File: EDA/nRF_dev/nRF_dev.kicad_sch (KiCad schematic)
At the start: 44 parts, among them J1 USB_B_Micro, J5 OV7675_DBG, J6 FH26W-25S-0.3SHW(60), U4 OV7675pcb

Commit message: working on nrf camera board
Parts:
- added J4, J7: Conn_01x08_Male, Connector_PinHeader_2.54mm:PinHeader_1x08_P2.54mm_Vertical, symbol Connector:Conn_01x08_Male
- added J8: Conn_01x32_Male, Connector_PinHeader_2.54mm:PinHeader_1x32_P2.54mm_Vertical, symbol Connector:Conn_01x32_Male
- added JP3: ., Jumper:SolderJumper-3_P1.3mm_Open_RoundedPad1.0x1.5mm, symbol Jumper:SolderJumper_3_Open
- added U1: 23LCV1024-I/SN, Package_SO:SOIC-8_3.9x4.9mm_P1.27mm, symbol project:23LCV1024-I/SN
- gave numbers to parts that had none: 29
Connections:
- net +BATT: now also JP3.3 (B)
- net -BATT: now also J4.1 (Pin_1), J4.3 (Pin_3), J4.5 (Pin_5), J4.7 (Pin_7), J7.1 (Pin_1), J7.3 (Pin_3), J7.5 (Pin_5), J7.7 (Pin_7), U1.4 (VSS), U1.7 (VBAT)
- net CB_D0: now also U3.95 (P0.00), J8.1 (Pin_1)
- net CB_D1: now also U3.96 (P0.01), J8.2 (Pin_2)
- net CB_D2: now also U3.97 (P0.02), J8.3 (Pin_3)
- net CB_D3: now also U3.99 (P0.03), J8.4 (Pin_4)
- net CB_D4: now also U3.100 (P0.04), J8.5 (Pin_5)
- net CB_D5: now also U3.2 (P0.05), J8.6 (Pin_6)
- net CB_D6: now also U3.3 (P0.06), J8.7 (Pin_7)
- net CB_D7: now also U3.4 (P0.07), J8.8 (Pin_8)
- net CB_VIN: now also U3.15 (P0.08), J8.9 (Pin_9)
- net FLASH_CS: now also U3.87 (P0.29), J8.30 (Pin_30)
- net FLASH_MISO: now also U3.84 (P0.27), J8.28 (Pin_28)
- net FLASH_MOSI: now also U3.86 (P0.28), J8.29 (Pin_29)
- net FLASH_SCLK: now also U3.83 (P0.26), J8.27 (Pin_27)
- net HREF: now also U3.20 (P0.12), J8.13 (Pin_13)
- net PCLK: now also U3.23 (P0.13_AIN0), J8.14 (Pin_14)
- net PDN: now also U3.26 (P0.16_AIN3), J8.17 (Pin_17)
- net PEN: now also U3.25 (P0.15_AIN2), J8.16 (Pin_16)
- net SCL: now also U3.16 (P0.09), J8.10 (Pin_10)
- net SDA: now also U3.18 (P0.10), J8.11 (Pin_11)
- net SD_CS: now also U3.42 (P0.25_TRACEDATA3), J8.26 (Pin_26), U1.1 (CS)
- net SD_MISO: now also U3.39 (P0.23_TRACEDATA1), J8.24 (Pin_24), U1.2 (SO)
- net SD_MOSI: now also U3.40 (P0.24_TRACEDATA2), J8.25 (Pin_25), U1.5 (SI)
- net SD_SCLK: now also U3.38 (P0.22_TRACEDATA0), J8.23 (Pin_23), U1.6 (SCK)
- net VPP: now also J4.2 (Pin_2), J4.4 (Pin_4), JP3.2 (C); no longer J1.1 (VBUS)
- net VS: now also U3.19 (P0.11), J8.12 (Pin_12)
- net V_3.3: now also J4.6 (Pin_6), J4.8 (Pin_8), J7.2 (Pin_2), J7.4 (Pin_4), J7.6 (Pin_6), J7.8 (Pin_8), U1.8 (VCC)
- net XCLK: now also U3.24 (P0.14_AIN1), J8.15 (Pin_15)
- net nRF_PWR: now also U3.88 (P0.30), J8.31 (Pin_31)
- net nRF_STAT: now also U3.89 (P0.31), J8.32 (Pin_32)
- net at U3.28 (P0.17_AIN4): now also J8.18 (Pin_18)
- net at U3.29 (P0.18_AIN5): now also J8.19 (Pin_19)
- net at U3.30 (P0.19_AIN6): now also J8.20 (Pin_20)
- net at U3.35 (P0.20_AIN7): now also J8.21 (Pin_21)
- net at U3.37 (P0.21_TRACECLK): now also J8.22 (Pin_22)
- new net V_USB: J1.1 (VBUS), JP3.1 (A)
- no-connect marks 50 -> 24
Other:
- moved on the sheet: C17, C3, J1, J2

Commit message: adding layout work for nrf_dev pcb
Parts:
- added J11: UART, Connector_PinHeader_2.54mm:PinHeader_1x04_P2.54mm_Vertical, symbol Connector_Generic:Conn_01x04
- added SW1: RST, Button_Switch_SMD:SW_Push_1P1T_NO_6x6mm_H9.5mm, symbol Switch:SW_SPST
- C1: value 100 μF -> 100 uF
- C17, C4: value 10u -> 10 uF
- C18, C19: value 100n -> 100 nF
- J1: footprint RP2040_minimal:USB_Micro-B_Amphenol_10103594-0001LF_Horizontal_modified -> Connector_USB:USB_Micro-B_Molex-105017-0001
- J10: footprint SIMFootprints:Pinpads_1.27mm02x03 -> Connector_PinHeader_1.27mm:PinHeader_2x03_P1.27mm_Vertical
- J2: footprint Connector_JST:JST_PH_S2B-PH-SM4-TB_1x02-1MP_P2.00mm_Horizontal -> Connector_BarrelJack:BarrelJack_Horizontal
- J3: footprint SIMFootprints:microSD_Connector -> project:microSD_Connector
- J9: footprint SIMFootprints:SIMNano -> project:SIMNano
- U5: footprint SIMFootprints:TSNP-6-2 -> project:TSNP-6-2
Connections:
- net +3V3 is gone; now on net V_3.3: C17.1, JP1.1 (A)
- net -BATT: now also J11.4 (Pin_4), SW1.1 (A)
- net FLASH_CS: now also U1.1 (CS)
- net FLASH_MISO: now also U1.2 (SO)
- net FLASH_MOSI: now also U1.5 (SI)
- net FLASH_SCLK: now also U1.6 (SCK)
- net SD_CS: no longer U1.1 (CS)
- net SD_MISO: no longer U1.2 (SO)
- net SD_MOSI: no longer U1.5 (SI)
- net SD_SCLK: no longer U1.6 (SCK)
- net nRF_RST: now also J11.3 (Pin_3), SW1.2 (B)
- net TX: now reaches J8.21 (Pin_21), U3.35 (P0.20_AIN7)
- net TX: now also J11.1 (Pin_1)
- net RX: now reaches J8.22 (Pin_22), U3.37 (P0.21_TRACECLK)
- net RX: now also J11.2 (Pin_2)
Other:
- note removed: "RTC"
- moved on the sheet: C5, C6, C8, C9

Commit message: more layout work
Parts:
- removed J8: Conn_01x32_Male, Connector_PinHeader_2.54mm:PinHeader_1x32_P2.54mm_Vertical, symbol Connector:Conn_01x32_Male
- added J8: Conn_01x15_Male, Connector_PinHeader_2.54mm:PinHeader_1x15_P2.54mm_Vertical, symbol Connector:Conn_01x15_Male
- added SW2: BTA, Button_Switch_SMD:SW_Push_1P1T_NO_6x6mm_H9.5mm, symbol Switch:SW_SPST
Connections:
- net nRF_PWR is gone; now on net RX: U3.88 (P0.30)
- net nRF_STAT is gone; now on net TX: U3.89 (P0.31)
- net -BATT: now also SW2.1 (A); no longer C17.2
- net CB_GND: now also C17.2
- net CB_VCC: now also C17.1, R2.1, R5.1
- net FLASH_CS: now also U3.86 (P0.28), J8.12 (Pin_12); no longer U3.87 (P0.29)
- net FLASH_MISO: now also U3.87 (P0.29), J8.13 (Pin_13); no longer U3.84 (P0.27)
- net FLASH_MOSI: now also U3.84 (P0.27), J8.11 (Pin_11); no longer U3.86 (P0.28)
- net FLASH_SCLK: now also J8.10 (Pin_10)
- net RX: now also J8.14 (Pin_14); no longer U3.37 (P0.21_TRACECLK)
- net SD_CS: now also J8.9 (Pin_9)
- net SD_MISO: now also J8.7 (Pin_7)
- net SD_MOSI: now also J8.8 (Pin_8)
- net SD_SCLK: now also J8.6 (Pin_6)
- net TX: now also J8.15 (Pin_15); no longer U3.35 (P0.20_AIN7)
- net V_3.3: no longer C17.1, R2.1, R5.1
- net at U3.28 (P0.17_AIN4): now also J8.1 (Pin_1)
- net at U3.29 (P0.18_AIN5): now also J8.2 (Pin_2)
- net at U3.30 (P0.19_AIN6): now also J8.3 (Pin_3)
- new net: J8.4 (Pin_4), U3.35 (P0.20_AIN7)
- new net BTA: J8.5 (Pin_5), SW2.2 (B), U3.37 (P0.21_TRACECLK)

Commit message: finished layout and gerber files for nRF dev camera
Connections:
- net -BATT: no longer J6.S1 (SHIELD), J6.S2 (SHIELD)
- net CB_GND: now also J6.S1 (SHIELD), J6.S2 (SHIELD)
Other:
- company: Raspberry Pi (Trading) Ltd -> BoSL
- title: RP2040 Minimal Design Example -> BoSL Camera dev
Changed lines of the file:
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@@
   (paper "A3")
   (title_block
-    (title "RP2040 Minimal Design Example")
-    (date "2020-12-18")
-    (rev "REV1")
-    (company "Raspberry Pi (Trading) Ltd")
+    (title "BoSL Camera dev")
+    (date "2022-11-06")
+    (rev "0.0.1")
+    (company "BoSL")
   )
   (junction (at 248.285 165.735) (diameter 0) (color 0 0 0 0)
@@
     (stroke (width 0) (type default) (color 0 0 0 0))
   )
-  (wire (pts (xy 255.27 258.445) (xy 255.27 260.985))
+  (wire (pts (xy 255.27 258.445) (xy 255.27 266.065))
     (stroke (width 0) (type default) (color 0 0 0 0))
   )
@@
     )
   )
+  (global_label "CB_GND" (shape input) (at 255.27 266.065 0) (fields_autoplaced)
+    (effects (font (size 1.27 1.27)) (justify left))
+    (property "Intersheet References" "${INTERSHEET_REFS}" (id 0) (at 264.9723 266.1444 0)
+      (effects (font (size 1.27 1.27)) (justify left) hide)
+    )
+  )
   (global_label "CB_D7" (shape input) (at 158.115 87.63 180) (fields_autoplaced)
     (effects (font (size 1.27 1.27)) (justify right))
@@
     (pin "2")
   )
-  (symbol (lib_id "power:GND") (at 255.27 260.985 0) (unit 1)
-    (in_bom yes) (on_board yes) (fields_autoplaced)
-    (property "Reference" "#PWR026" (id 0) (at 255.27 267.335 0)
-      (effects (font (size 1.27 1.27)) hide)
-    )
-    (property "Value" "GND" (id 1) (at 255.27 265.5475 0))
-    (property "Footprint" "" (id 2) (at 255.27 260.985 0)
-      (effects (font (size 1.27 1.27)) hide)
-    )
-    (property "Datasheet" "" (id 3) (at 255.27 260.985 0)
-      (effects (font (size 1.27 1.27)) hide)
-    )
-    (pin "1")
-  )
   (symbol (lib_id "BoSLnano-rescue:GND-power") (at 398.78 108.585 0) (unit 1)
     (in_bom yes) (on_board yes)
@@
       (reference "#PWR010") (unit 1) (value "GND") (footprint "")
     )
-    (path "/41dbed34-9b8b-45d8-83ff-788619bc7781"
-      (reference "#PWR026") (unit 1) (value "GND") (footprint "")
-    )
     (path "/37f37914-e8e7-48b3-9784-24b435a1454c"

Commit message: fixed pcb errors
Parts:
- removed R6: 1 kΩ, Resistor_SMD:R_0402_1005Metric, symbol BoSLnano-rescue:R-Device
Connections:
- net VPP: now also R4.1
- net V_3.3: no longer R4.1
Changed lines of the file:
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@@
   (title_block
     (title "BoSL Camera dev")
-    (date "2022-11-06")
-    (rev "0.0.1")
+    (date "2022-11-23")
+    (rev "0.0.2")
     (company "BoSL")
   )
@@
   (junction (at 172.72 133.35) (diameter 0) (color 0 0 0 0)
   )
-  (junction (at 229.87 93.345) (diameter 0) (color 0 0 0 0)
-  )
   (junction (at 353.06 95.885) (diameter 0) (color 0 0 0 0)
   )
@@
     (stroke (width 0) (type default) (color 0 0 0 0))
   )
-  (wire (pts (xy 229.87 93.345) (xy 239.395 93.345))
-    (stroke (width 0) (type default) (color 0 0 0 0))
-  )
   (wire (pts (xy 172.72 135.89) (xy 175.26 135.89))
     (stroke (width 0) (type default) (color 0 0 0 0))
@@
     (stroke (width 0) (type default) (color 0 0 0 0))
   )
-  (wire (pts (xy 326.39 169.545) (xy 326.39 163.83))
-    (stroke (width 0) (type default) (color 0 0 0 0))
-  )
   (wire (pts (xy 394.97 98.425) (xy 398.78 98.425))
     (stroke (width 0) (type default) (color 0 0 0 0))
@@
     (stroke (width 0) (type default) (color 0 0 0 0))
   )
-  (wire (pts (xy 239.395 93.345) (xy 239.395 97.155))
+  (wire (pts (xy 239.395 95.25) (xy 239.395 97.155))
     (stroke (width 0) (type default) (color 0 0 0 0))
   )
@@
     )
   )
-  (global_label "V_3.3" (shape input) (at 326.39 156.21 90) (fields_autoplaced)
-    (effects (font (size 1.524 1.524)) (justify left))
-    (property "Intersheet References" "${INTERSHEET_REFS}" (id 0) (at 275.59 -10.16 0)
-      (effects (font (size 1.27 1.27)) hide)
-    )
-  )
   (global_label "SCL" (shape input) (at 266.7 238.125 0) (fields_autoplaced)
     (effects (font (size 1.27 1.27)) (justify left))
@@
     (pin "1")
   )
-  (symbol (lib_id "BoSLnano-rescue:R-Device") (at 326.39 160.02 0) (unit 1)
-    (in_bom yes) (on_board yes)
-    (property "Reference" "R6" (id 0) (at 323.215 159.385 0))
-    (property "Value" "1 kΩ" (id 1) (at 321.945 161.925 0))
-    (property "Footprint" "Resistor_SMD:R_0402_1005Metric" (id 2) (at 324.612 160.02 90)
-      (effects (font (size 1.27 1.27)) hide)
-    )
-    (property "Datasheet" "" (id 3) (at 326.39 160.02 0))
-    (pin "1")
-    (pin "2")
-  )
   (symbol (lib_id "SIM7000-rescue:AT-ant") (at 290.195 87.63 270) (mirror x) (unit 1)
     (in_bom yes) (on_board yes)
@@
     (pin "2")
   )
+  (symbol (lib_id "BoSLnano-rescue:VPP-power") (at 239.395 95.25 0) (unit 1)
+    (in_bom yes) (on_board yes)
+    (property "Reference" "#PWR0103" (id 0) (at 239.395 99.06 0)
+      (effects (font (size 1.27 1.27)) hide)
+    )
+    (property "Value" "VPP" (id 1) (at 239.395 91.44 0))
+    (property "Footprint" "" (id 2) (at 239.395 95.25 0))
+    (property "Datasheet" "" (id 3) (at 239.395 95.25 0))
+    (pin "1")
+  )
   (symbol (lib_id "BoSLnano-rescue:Micro_SD_Card-Connector") (at 48.895 137.16 180) (unit 1)
     (in_bom yes) (on_board yes)
@@
     (pin "97")
     (pin "99")
+    (pin "1")
+    (pin "10")
+    (pin "104")
+    (pin "105")
+    (pin "106")
+    (pin "107")
+    (pin "108")
+    (pin "109")
+    (pin "11")
+    (pin "110")
+    (pin "111")
+    (pin "112")
+    (pin "113")
+    (pin "114")
+    (pin "115")
+    (pin "116")
+    (pin "117")
+    (pin "118")
+    (pin "119")
+    (pin "120")
+    (pin "121")
+    (pin "122")
+    (pin "123")
+    (pin "124")
+    (pin "125")
+    (pin "126")
+    (pin "127")
+    (pin "14")
+    (pin "17")
+    (pin "21")
+    (pin "27")
+    (pin "31")
+    (pin "36")
+    (pin "41")
+    (pin "44")
+    (pin "47")
+    (pin "5")
+    (pin "50")
+    (pin "51")
+    (pin "52")
+    (pin "56")
+    (pin "6")
+    (pin "60")
+    (pin "62")
+    (pin "63")
+    (pin "65")
+    (pin "66")
+    (pin "68")
+    (pin "69")
+    (pin "7")
+    (pin "70")
+    (pin "71")
+    (pin "72")
+    (pin "73")
+    (pin "74")
+    (pin "75")
+    (pin "76")
+    (pin "77")
+    (pin "78")
+    (pin "79")
+    (pin "8")
+    (pin "80")
+    (pin "81")
+    (pin "82")
+    (pin "85")
+    (pin "9")
+    (pin "90")
+    (pin "94")
+    (pin "98")
   )
   (symbol (lib_id "BoSLnano-rescue:CP-Device") (at 58.42 49.53 0) (unit 1)
@@
       (effects (font (size 1.524 1.524)) hide)
     )
+    (pin "100")
+    (pin "101")
+    (pin "102")
+    (pin "103")
+    (pin "12")
+    (pin "13")
+    (pin "15")
+    (pin "16")
+    (pin "18")
+    (pin "19")
+    (pin "2")
+    (pin "20")
+    (pin "22")
+    (pin "23")
+    (pin "24")
+    (pin "25")
+    (pin "26")
+    (pin "28")
+    (pin "29")
+    (pin "3")
+    (pin "30")
+    (pin "32")
+    (pin "33")
+    (pin "34")
+    (pin "35")
+    (pin "37")
+    (pin "38")
+    (pin "39")
+    (pin "4")
+    (pin "40")
+    (pin "42")
+    (pin "43")
+    (pin "45")
+    (pin "46")
+    (pin "48")
+    (pin "49")
+    (pin "53")
+    (pin "54")
+    (pin "55")
+    (pin "57")
+    (pin "58")
+    (pin "59")
+    (pin "61")
+    (pin "64")
+    (pin "67")
+    (pin "83")
+    (pin "84")
+    (pin "86")
+    (pin "87")
+    (pin "88")
+    (pin "89")
+    (pin "91")
+    (pin "92")
+    (pin "93")
+    (pin "95")
+    (pin "96")
+    (pin "97")
+    (pin "99")
     (pin "1")
     (pin "10")
@@
       (reference "#PWR0102") (unit 1) (value "GND") (footprint "")
     )
+    (path "/13496581-9c4a-4023-97de-a6a6bad5a40f"
+      (reference "#PWR0103") (unit 1) (value "VPP") (footprint "")
+    )
     (path "/cbf8ffc8-8d47-4a8d-b9de-646161a7b2a8"
       (reference "#PWR0104") (unit 1) (value "GND") (footprint "")
@@
       (reference "R5") (unit 1) (value "10 kΩ") (footprint "Resistor_SMD:R_0402_1005Metric")
     )
-    (path "/127d9ee2-01d1-498f-ae61-5e2a7396948b"
-      (reference "R6") (unit 1) (value "1 kΩ") (footprint "Resistor_SMD:R_0402_1005Metric")
-    )
     (path "/f5d5bd4a-108f-418f-8859-779e2f50ba63"

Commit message: revision 0.0.3 of the nRF dev board
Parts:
- added D1: LED, LED_SMD:LED_0603_1608Metric_Pad1.05x0.95mm_HandSolder, symbol Device:LED
- added R6, R8: 10 kΩ, Resistor_SMD:R_0402_1005Metric, symbol BoSLnano-rescue:R-Device
- added U7: SIP32508DT-T1-GE3, Package_TO_SOT_SMD:SOT-23-6, symbol project:SIP32508DT-T1-GE3
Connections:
- net -BATT: now also D1.1 (K), U7.4 (GND)
- net CB_D0: now also J5.16 (Pin_16), J6.22, U4.16 (D1); no longer J5.15 (Pin_15), J6.4, U4.15 (D0)
- net CB_D1: now also J5.15 (Pin_15), J6.21, U4.15 (D0); no longer J5.16 (Pin_16), J6.5, U4.16 (D1)
- net CB_D2: now also J6.20; no longer J6.6
- net CB_D3: now also J6.19; no longer J6.7
- net CB_D4: now also J6.18; no longer J6.8
- net CB_D5: now also J6.17; no longer J6.9
- net CB_D6: now also J6.16; no longer J6.10
- net CB_D7: now also J6.15; no longer J6.11
- net CB_GND: now also J6.12, J6.8; no longer J6.14, J6.18
- net CB_VCC: now also J6.6, J6.7; no longer J6.19, J6.20
- net HREF: now also J6.10; no longer J6.16
- net PCLK: now also J6.9; no longer J6.17
- net PDN: now also J6.1; no longer J6.25
- net SCL: now also J6.14; no longer J6.12
- net VS: now also J6.5; no longer J6.21
- net V_3.3: now also U7.5 (IN), U7.6 (IN)
- net XCLK: now also J6.11; no longer J6.15
- net LED: now reaches J8.4 (Pin_4), U3.35 (P0.20_AIN7)
- net LED: now also R6.1, R8.1
- net CB_VIN: no longer names the net of JP1.3 (B)
- net CB_VIN: now also U7.1 (OUT), U7.2 (OUT); no longer U3.15 (P0.08)
- new net: D1.2 (A), R6.2, R8.2
- new net CB_VEN: U3.15 (P0.08), U7.3 (EN)
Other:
- moved on the sheet: C17, C18, C19, J6, JP1, JP2, R2, R5, SW1, SW2

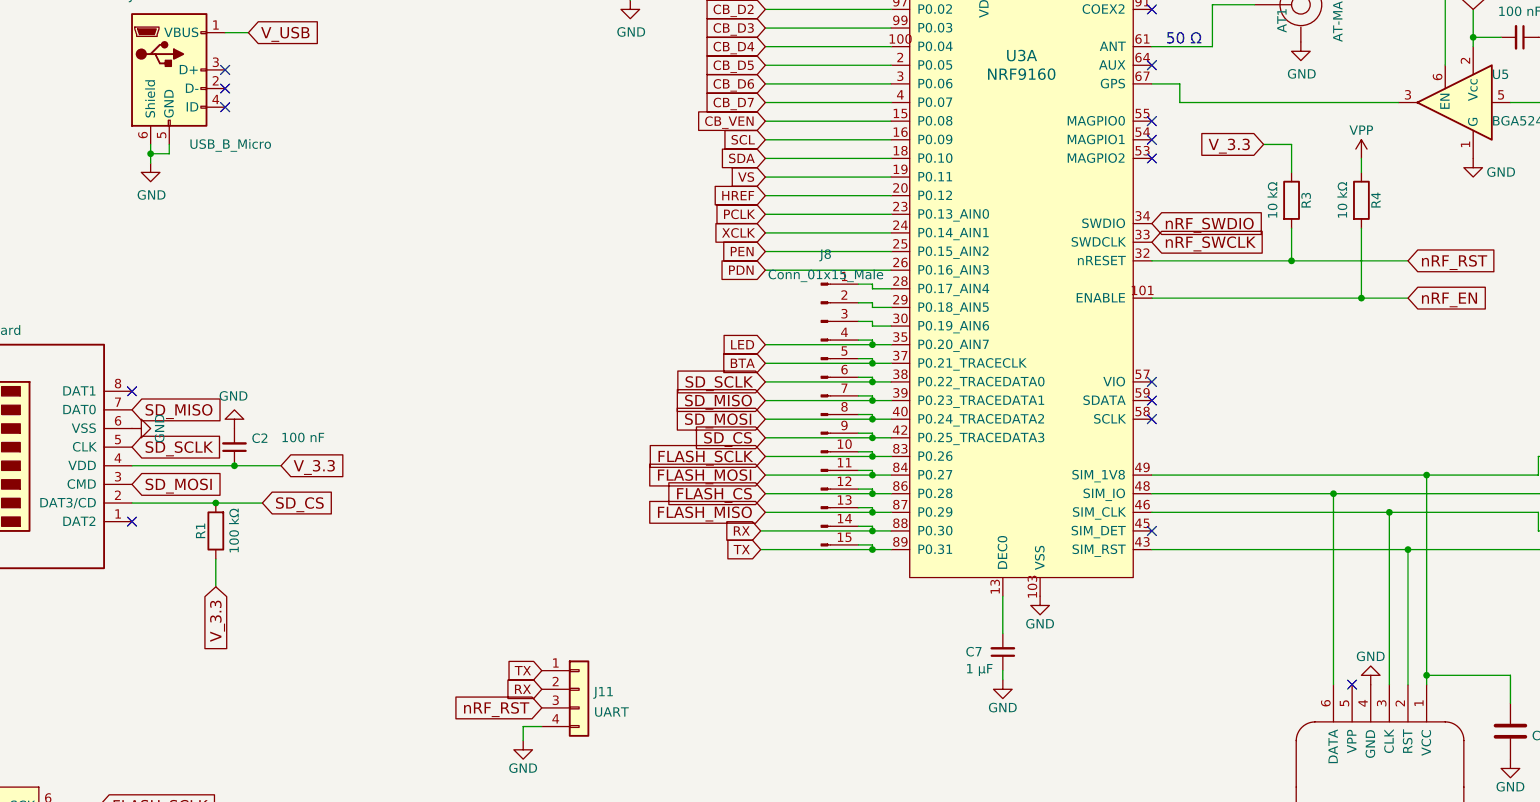
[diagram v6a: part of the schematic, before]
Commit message: updated power saving features
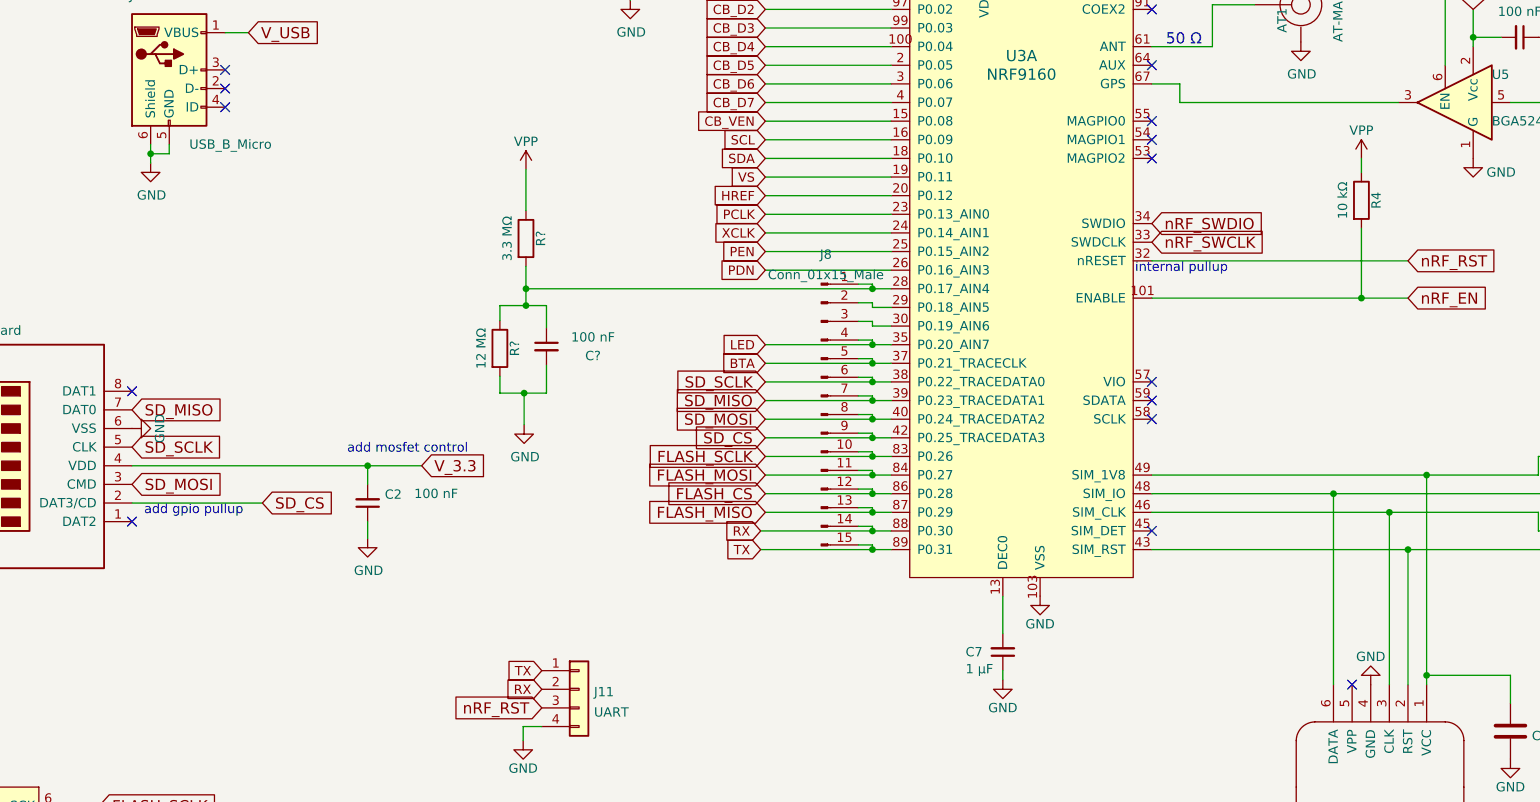
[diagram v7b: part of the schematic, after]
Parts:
- removed R1: 100 kΩ, Resistor_SMD:R_0402_1005Metric, symbol BoSLnano-rescue:R-Device
- removed R3: 10 kΩ, Resistor_SMD:R_0402_1005Metric, symbol BoSLnano-rescue:R-Device
- added C?: 100 nF, Capacitor_SMD:C_0402_1005Metric, symbol BoSLnano-rescue:C_Small-Device
- added R?: 3.3 MΩ, Resistor_SMD:R_0402_1005Metric, symbol BoSLnano-rescue:R-Device
- added R?: 12 MΩ, Resistor_SMD:R_0402_1005Metric, symbol BoSLnano-rescue:R-Device
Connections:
- net -BATT: now also C2.1, C?.2, R?.2; no longer C2.2
- net VPP: now also R?.1
- net V_3.3: now also C2.2; no longer C2.1
- net at J8.1 (Pin_1), U3.28 (P0.17_AIN4): now also C?.1, R?.1, R?.2
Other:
- note added: "add gpio pullup"
- note added: "add mosfet control"
- note added: "internal pullup"
- moved on the sheet: C2
